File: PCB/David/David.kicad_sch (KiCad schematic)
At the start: 2 parts, among them J1 Conn_01x15_Socket, J2 Conn_01x15_Socket

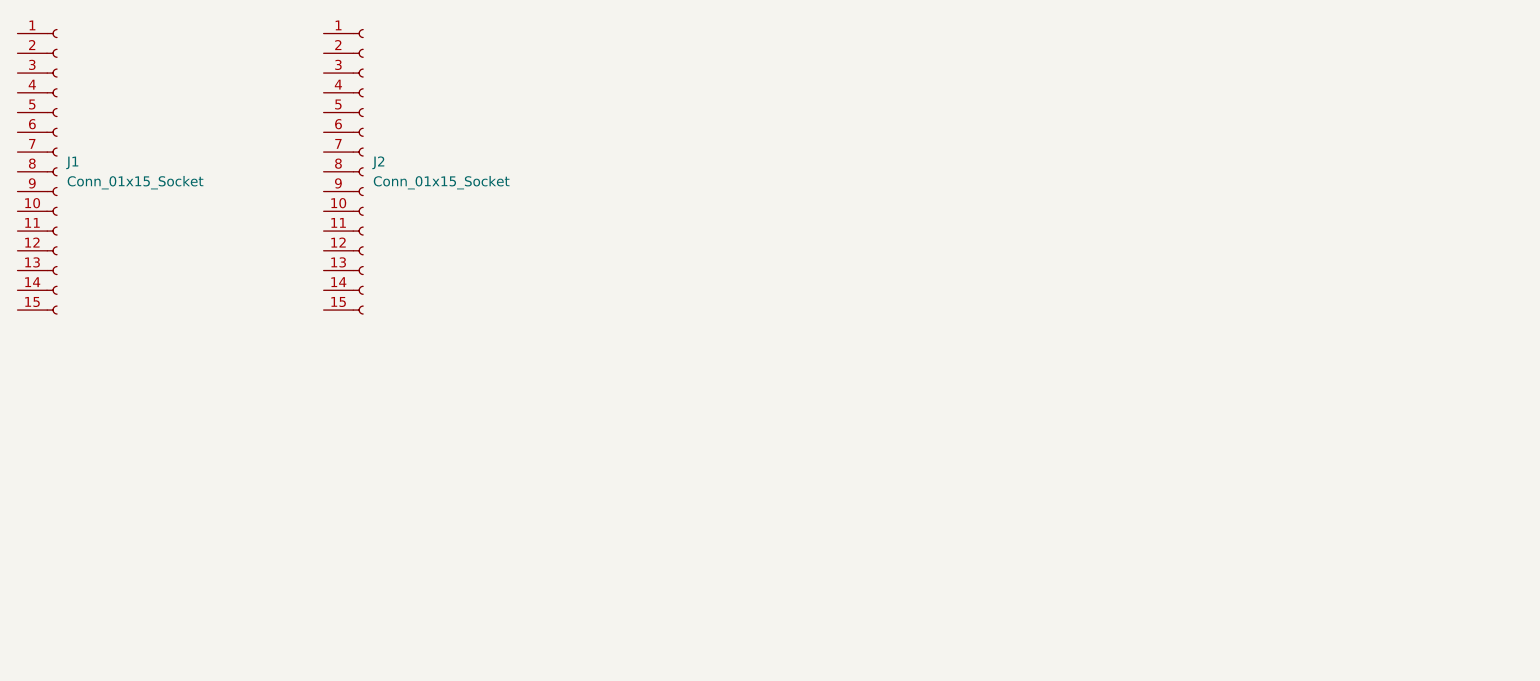
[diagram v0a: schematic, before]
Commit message: Updated 3D models
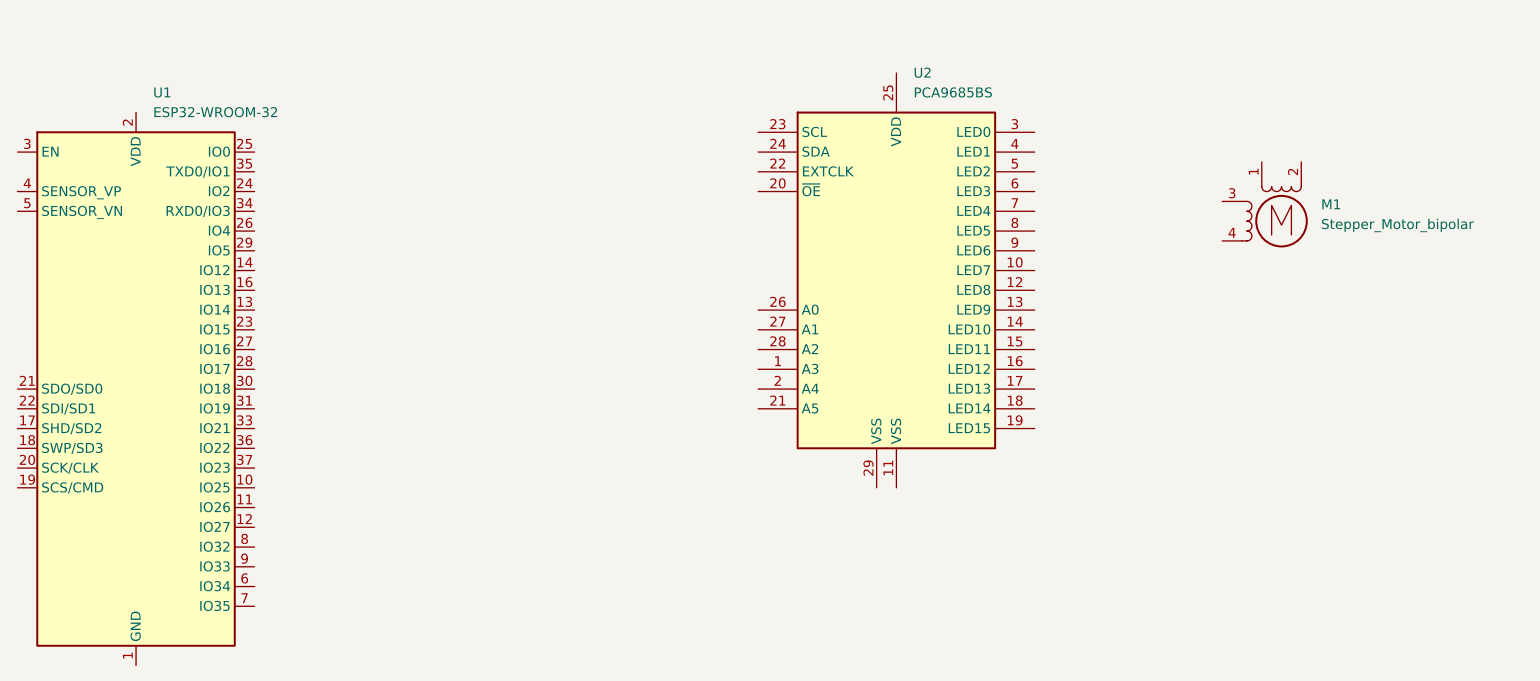
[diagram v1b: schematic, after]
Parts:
- removed J1, J2: Conn_01x15_Socket, symbol Connector:Conn_01x15_Socket
- added M1: Stepper_Motor_bipolar, symbol Motor:Stepper_Motor_bipolar
- added U1: ESP32-WROOM-32, RF_Module:ESP32-WROOM-32, symbol RF_Module:ESP32-WROOM-32
- added U2: PCA9685BS, Package_DFN_QFN:QFN-28-1EP_6x6mm_P0.65mm_EP4.25x4.25mm, symbol Driver_LED:PCA9685BS
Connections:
- new net: U1.1 (GND), U1.15 (GND), U1.38 (GND), U1.39 (GND)
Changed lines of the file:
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@@
 	(paper "A4")
 	(symbol
-		(lib_id "Connector:Conn_01x15_Socket")
-		(at 93.98 46.99 0)
+		(lib_id "Motor:Stepper_Motor_bipolar")
+		(at 251.46 53.34 0)
 		(unit 1)
 		(exclude_from_sim no)
@@
 		(dnp no)
 		(fields_autoplaced yes)
-		(property "Reference" "J1"
-			(at 95.25 45.7199 0)
-			(effects
-				(font
-					(size 1.27 1.27)
-				)
-				(justify left)
-			)
-		)
-		(property "Value" "Conn_01x15_Socket"
-			(at 95.25 48.2599 0)
+		(property "Reference" "M1"
+			(at 256.54 51.219 0)
+			(effects
+				(font
+					(size 1.27 1.27)
+				)
+				(justify left)
+			)
+		)
+		(property "Value" "Stepper_Motor_bipolar"
+			(at 256.54 53.759 0)
 			(effects
 				(font
@@
 		)
 		(property "Footprint" ""
-			(at 93.98 46.99 0)
-			(effects
-				(font
-					(size 1.27 1.27)
-				)
-				(hide yes)
-			)
-		)
-		(property "Datasheet" "~"
-			(at 93.98 46.99 0)
-			(effects
-				(font
-					(size 1.27 1.27)
-				)
-				(hide yes)
-			)
-		)
-		(property "Description" "Generic connector, single row, 01x15, script generated"
-			(at 93.98 46.99 0)
-			(effects
-				(font
-					(size 1.27 1.27)
-				)
-				(hide yes)
-			)
-		)
-		(pin "7"
-		)
-		(pin "12"
-		)
-		(pin "6"
+			(at 251.714 53.594 0)
+			(effects
+				(font
+					(size 1.27 1.27)
+				)
+				(hide yes)
+			)
+		)
+		(property "Datasheet" "http://www.infineon.com/dgdl/Application-Note-TLE8110EE_driving_UniPolarStepperMotor_V1.1.pdf?fileId=db3a30431be39b97011be5d0aa0a00b0"
+			(at 251.714 53.594 0)
+			(effects
+				(font
+					(size 1.27 1.27)
+				)
+				(hide yes)
+			)
+		)
+		(property "Description" "4-wire bipolar stepper motor"
+			(at 251.46 53.34 0)
+			(effects
+				(font
+					(size 1.27 1.27)
+				)
+				(hide yes)
+			)
+		)
+		(pin "2"
+		)
+		(pin "3"
+		)
+		(pin "4"
 		)
 		(pin "1"
-		)
-		(pin "10"
-		)
-		(pin "15"
-		)
-		(pin "8"
-		)
-		(pin "14"
-		)
-		(pin "13"
-		)
-		(pin "2"
-		)
-		(pin "4"
-		)
-		(pin "11"
-		)
-		(pin "5"
-		)
-		(pin "3"
-		)
-		(pin "9"
 		)
 		(instances
 			(project "David"
 				(path "/fb415cfd-cf51-4a2f-9e3f-63b4b2e0ca71"
-					(reference "J1")
+					(reference "M1")
 					(unit 1)
 				)
@@
 	)
 	(symbol
-		(lib_id "Connector:Conn_01x15_Socket")
-		(at 133.35 46.99 0)
+		(lib_id "RF_Module:ESP32-WROOM-32")
+		(at 104.14 74.93 0)
 		(unit 1)
 		(exclude_from_sim no)
@@
 		(dnp no)
 		(fields_autoplaced yes)
-		(property "Reference" "J2"
-			(at 134.62 45.7199 0)
-			(effects
-				(font
-					(size 1.27 1.27)
-				)
-				(justify left)
-			)
-		)
-		(property "Value" "Conn_01x15_Socket"
-			(at 134.62 48.2599 0)
-			(effects
-				(font
-					(size 1.27 1.27)
-				)
-				(justify left)
-			)
-		)
-		(property "Footprint" ""
-			(at 133.35 46.99 0)
-			(effects
-				(font
-					(size 1.27 1.27)
-				)
-				(hide yes)
-			)
-		)
-		(property "Datasheet" "~"
-			(at 133.35 46.99 0)
-			(effects
-				(font
-					(size 1.27 1.27)
-				)
-				(hide yes)
-			)
-		)
-		(property "Description" "Generic connector, single row, 01x15, script generated"
-			(at 133.35 46.99 0)
-			(effects
-				(font
-					(size 1.27 1.27)
-				)
-				(hide yes)
-			)
+		(property "Reference" "U1"
+			(at 106.3341 36.83 0)
+			(effects
+				(font
+					(size 1.27 1.27)
+				)
+				(justify left)
+			)
+		)
+		(property "Value" "ESP32-WROOM-32"
+			(at 106.3341 39.37 0)
+			(effects
+				(font
+					(size 1.27 1.27)
+				)
+				(justify left)
+			)
+		)
+		(property "Footprint" "RF_Module:ESP32-WROOM-32"
+			(at 104.14 113.03 0)
+			(effects
+				(font
+					(size 1.27 1.27)
+				)
+				(hide yes)
+			)
+		)
+		(property "Datasheet" "https://www.espressif.com/sites/default/files/documentation/esp32-wroom-32_datasheet_en.pdf"
+			(at 96.52 73.66 0)
+			(effects
+				(font
+					(size 1.27 1.27)
+				)
+				(hide yes)
+			)
+		)
+		(property "Description" "RF Module, ESP32-D0WDQ6 SoC, Wi-Fi 802.11b/g/n, Bluetooth, BLE, 32-bit, 2.7-3.6V, onboard antenna, SMD"
+			(at 104.14 74.93 0)
+			(effects
+				(font
+					(size 1.27 1.27)
+				)
+				(hide yes)
+			)
+		)
+		(pin "6"
+		)
+		(pin "10"
+		)
+		(pin "13"
+		)
+		(pin "14"
+		)
+		(pin "20"
+		)
+		(pin "3"
+		)
+		(pin "31"
+		)
+		(pin "35"
+		)
+		(pin "23"
+		)
+		(pin "4"
+		)
+		(pin "5"
+		)
+		(pin "28"
+		)
+		(pin "16"
+		)
+		(pin "38"
+		)
+		(pin "36"
+		)
+		(pin "1"
+		)
+		(pin "27"
+		)
+		(pin "15"
+		)
+		(pin "30"
+		)
+		(pin "33"
+		)
+		(pin "37"
+		)
+		(pin "24"
+		)
+		(pin "29"
+		)
+		(pin "25"
+		)
+		(pin "32"
+		)
+		(pin "17"
+		)
+		(pin "18"
+		)
+		(pin "8"
+		)
+		(pin "22"
+		)
+		(pin "26"
+		)
+		(pin "39"
+		)
+		(pin "21"
+		)
+		(pin "34"
+		)
+		(pin "12"
+		)
+		(pin "11"
+		)
+		(pin "19"
+		)
+		(pin "2"
 		)
 		(pin "7"
-		)
-		(pin "12"
-		)
-		(pin "6"
-		)
-		(pin "1"
-		)
-		(pin "10"
-		)
-		(pin "15"
-		)
-		(pin "8"
-		)
-		(pin "14"
-		)
-		(pin "13"
-		)
-		(pin "2"
-		)
-		(pin "4"
-		)
-		(pin "11"
-		)
-		(pin "5"
-		)
-		(pin "3"
 		)
 		(pin "9"
@@
 			(project "David"
 				(path "/fb415cfd-cf51-4a2f-9e3f-63b4b2e0ca71"
-					(reference "J2")
+					(reference "U1")
 					(unit 1)
 				)
+			)
+		)
+	)
+	(symbol
+		(lib_id "Driver_LED:PCA9685BS")
+		(at 201.93 59.69 0)
+		(unit 1)
+		(exclude_from_sim no)
+		(in_bom yes)
+		(on_board yes)
+		(dnp no)
+		(fields_autoplaced yes)
+		(property "Reference" "U2"
+			(at 204.1241 34.29 0)
+			(effects
+				(font
+					(size 1.27 1.27)
+				)
+				(justify left)
+			)
+		)
+		(property "Value" "PCA9685BS"
+			(at 204.1241 36.83 0)
+			(effects
+				(font
+					(size 1.27 1.27)
+				)
+				(justify left)
+			)
+		)
+		(property "Footprint" "Package_DFN_QFN:QFN-28-1EP_6x6mm_P0.65mm_EP4.25x4.25mm"
+			(at 202.565 84.455 0)
+			(effects
+				(font
+					(size 1.27 1.27)
+				)
+				(justify left)
+				(hide yes)
+			)
+		)
+		(property "Datasheet" "http://www.nxp.com/docs/en/data-sheet/PCA9685.pdf"
+			(at 191.77 41.91 0)
+			(effects
+				(font
+					(size 1.27 1.27)
+				)
+				(hide yes)
+			)
+		)
+		(property "Description" "16-channel 12-bit PWM Fm+ I2C-bus LED controller RGBA QFN"
+			(at 201.93 59.69 0)
+			(effects
+				(font
+					(size 1.27 1.27)
+				)
+				(hide yes)
+			)
+		)
+		(pin "11"
+		)
+		(pin "1"
+		)
+		(pin "10"
+		)
+		(pin "14"
+		)
+		(pin "16"
+		)
+		(pin "17"
+		)
+		(pin "18"
+		)
+		(pin "19"
+		)
+		(pin "2"
+		)
+		(pin "20"
+		)
+		(pin "21"
+		)
+		(pin "13"
+		)
+		(pin "12"
+		)
+		(pin "15"
+		)
+		(pin "23"
+		)
+		(pin "24"
+		)
+		(pin "25"
+		)
+		(pin "22"
+		)
+		(pin "26"
+		)
+		(pin "9"
+		)
+		(pin "3"
+		)
+		(pin "4"
+		)
+		(pin "29"
+		)
+		(pin "5"
+		)
+		(pin "6"
+		)
+		(pin "27"
+		)
+		(pin "7"
+		)
+		(pin "8"
+		)
+		(pin "28"
+		)
+		(instances
+			(project "David"
+				(path "/fb415cfd-cf51-4a2f-9e3f-63b4b2e0ca71"
+					(reference "U2")
+					(unit 1)
+				)
